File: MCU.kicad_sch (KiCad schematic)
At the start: 12 parts, among them SW1 KMR221NGLFS, U1 STM32L432KCUx

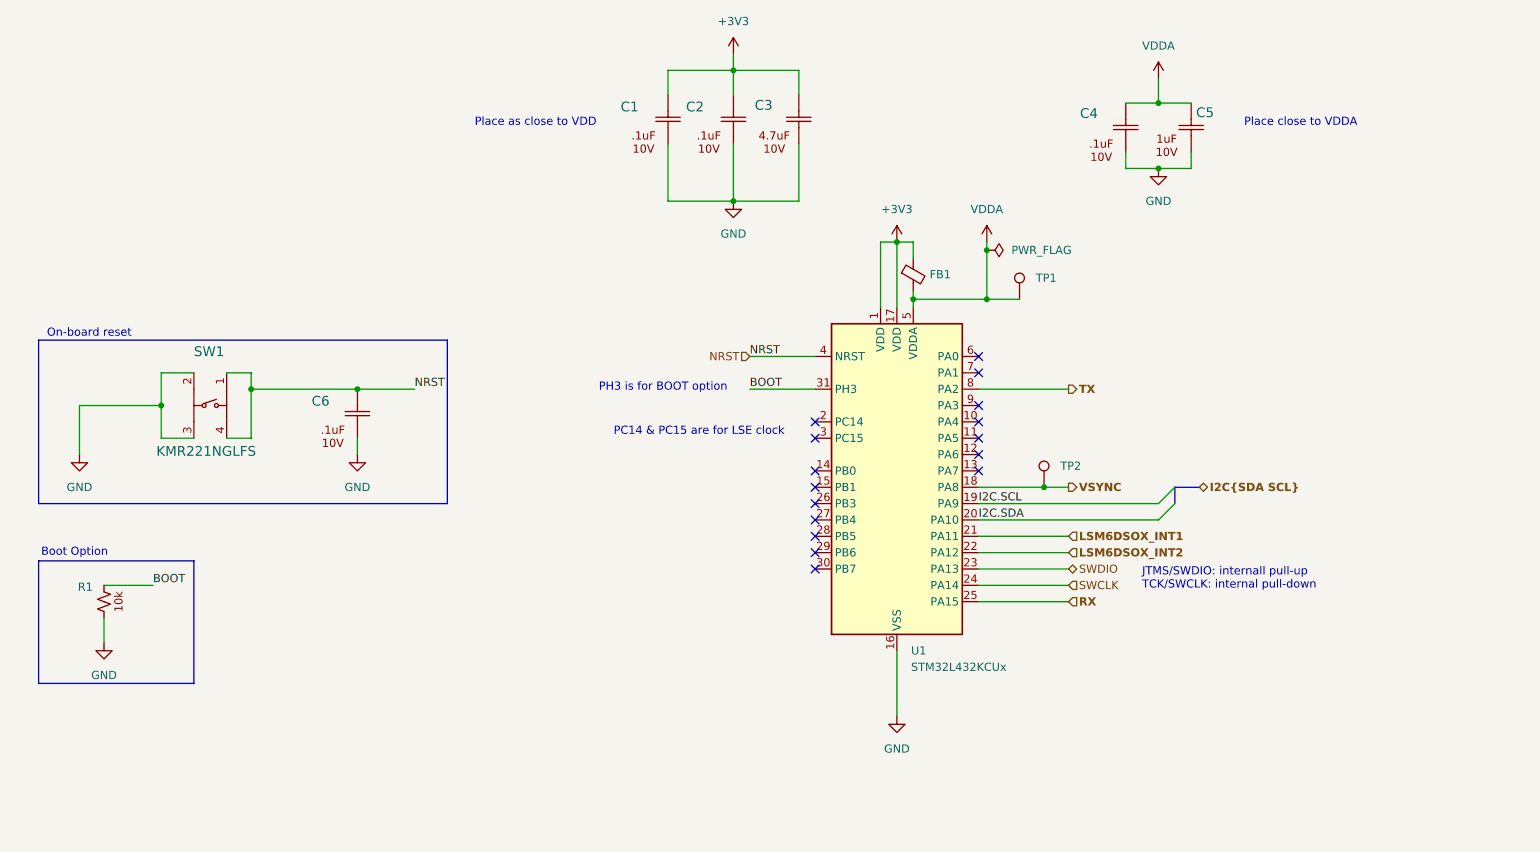
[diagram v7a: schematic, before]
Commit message: Addressed pull-up on NRST. Added GPIO for  VIO_EN. Added comments on schematic and some TPs
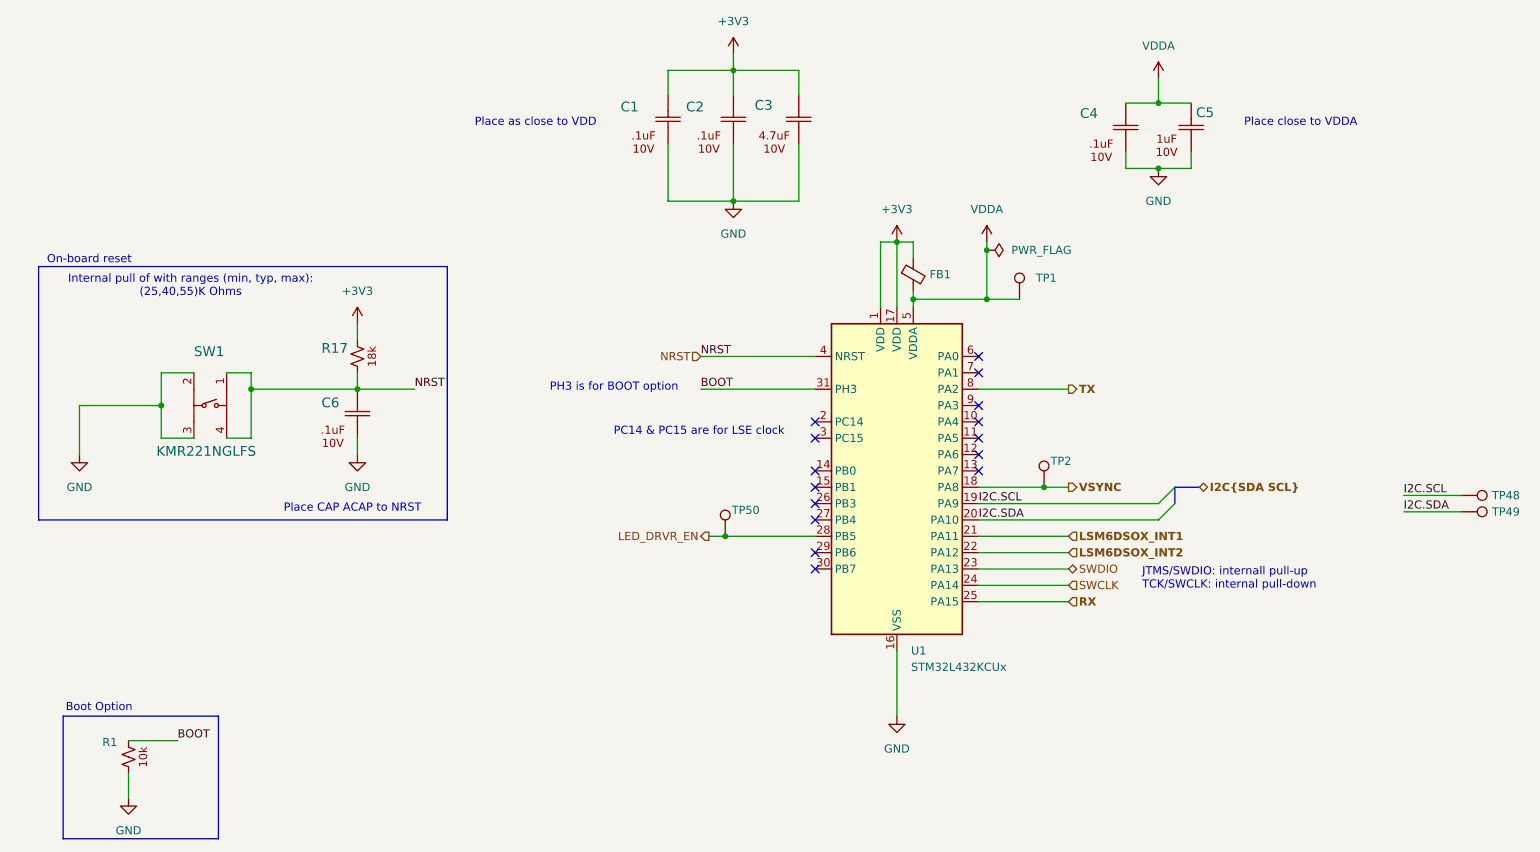
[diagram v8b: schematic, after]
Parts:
- added R17: CRCW080518K0FKEAHP, Hourglass_footprint_library:CRCW080518K0FKEAHP, symbol Hourglass_symbol_library:CRCW080518K0FKEAHP
- added TP48, TP49, TP50: TestPoint, TestPoint:TestPoint_Pad_D1.0mm, symbol Connector:TestPoint
- FB1: value FerriteBead_Small -> FCM 1608KF-601T03
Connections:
- net +3V3: now also R17.2
- net I2C.SCL: now also TP48.1
- net I2C.SDA: now also TP49.1
- net NRST: now also R17.1
- net LED_DRVR_EN: now reaches U1.28 (PB5)
- net LED_DRVR_EN: now also TP50.1
- no-connect marks 16 -> 15
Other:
- note added: "Internal pull of with ranges (min, typ, max): (25,40,55)K Ohms"
- note added: "Place CAP ACAP to NRST"
- moved on the sheet: R1
